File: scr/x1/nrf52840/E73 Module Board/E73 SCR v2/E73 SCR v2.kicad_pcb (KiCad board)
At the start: 4 copper layers, 50 x 35 mm, 36 parts, among them J1 SWD, J2 USB_B_Micro, J3 XC1, J4 XC2, J5 XC3, J6 BAT, Q1 AO3401, SW1 SW_BAT, U1 E73-2G4M08S1C-52840, U2 MCP73831-2-OT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

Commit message: Auto stash before merge of "footprint_update" and "origin/footprint_update"
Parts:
- RST1: footprint Switches:Tac_SPST_RightAngle_SideActuated_THT -> Switches:Tac_SMD_6.4mm_Side_SPST_NO
- moved RST1 22.5 mm to (71.2, 122.5)
- moved R6 4.37 mm to (112.0, 103.5), turned to 180 degrees
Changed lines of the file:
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@@
     (add_net "Net-(D1-Pad3)")
     (add_net "Net-(D2-Pad1)")
+    (add_net "Net-(D3-Pad1)")
     (add_net "Net-(D4-Pad1)")
+    (add_net "Net-(J1-Pad6)")
+    (add_net "Net-(J1-Pad7)")
+    (add_net "Net-(J1-Pad8)")
+    (add_net "Net-(J2-Pad4)")
     (add_net "Net-(J2-Pad6)")
     (add_net "Net-(R7-Pad2)")
@@
     (add_net P1.02)
     (add_net P1.09)
+    (add_net P1_11)
     (add_net RESET)
     (add_net SPKR)
@@
     (uvia_drill 0.1)
     (add_net VBUS)
+  )
+  (module Switches:Tac_SMD_6.4mm_Side_SPST_NO (layer F.Cu)
+    (at 71.25 122.5)
+    (descr "side smd tac switch")
+    (tags "switch tac rightangle side smd")
+    (attr smd)
+    (fp_text reference RST1 (at 0 0) (layer F.Fab)
+      (effects (font (size 1 1) (thickness 0.15)))
+    )
+    (fp_text value SW_SPST (at 0 -2.7) (layer F.Fab)
+      (effects (font (size 1 1) (thickness 0.15)))
+    )
+    (fp_line (start -1.3 2.5) (end 1.3 2.5) (layer Eco1.User) (width 0.15))
+    (fp_line (start 1.3 2.75) (end 1.3 1.75) (layer Eco1.User) (width 0.15))
+    (fp_line (start -1.3 2.75) (end 1.3 2.75) (layer Eco1.User) (width 0.15))
+    (fp_line (start -1.3 1.75) (end -1.3 2.75) (layer Eco1.User) (width 0.15))
+    (fp_line (start -3.4 1.75) (end -3.4 -1.7) (layer F.SilkS) (width 0.15))
+    (fp_line (start 3.4 1.75) (end -3.4 1.75) (layer F.SilkS) (width 0.15))
+    (fp_line (start 3.4 -1.75) (end 3.4 1.75) (layer F.SilkS) (width 0.15))
+    (fp_line (start -3.4 -1.75) (end 3.4 -1.75) (layer F.SilkS) (width 0.15))
+    (pad 1 smd rect (at 2.8 -0.85) (size 1.2 1) (layers F.Cu F.Paste F.Mask)
+      (net 1 GND))
+    (pad 2 smd rect (at 2.8 0.85) (size 1.2 1) (layers F.Cu F.Paste F.Mask)
+      (net 10 RESET))
+    (pad 2 smd rect (at -2.8 0.85) (size 1.2 1) (layers F.Cu F.Paste F.Mask)
+      (net 10 RESET))
+    (pad 1 smd rect (at -2.8 -0.75) (size 1.2 1) (layers F.Cu F.Paste F.Mask)
+      (net 1 GND))
+    (pad "" np_thru_hole circle (at 0 1.375) (size 0.75 0.75) (drill 0.75) (layers *.Cu *.Mask))
+    (pad "" np_thru_hole circle (at 0 -1.375) (size 0.75 0.75) (drill 0.75) (layers *.Cu *.Mask))
   )
   (module BVH_Components_Misc:SMD_Speaker (layer F.Cu)
@@
       (net 1 GND))
   )
-  (module Switches:Tac_SPST_RightAngle_SideActuated_THT (layer F.Cu)
-    (at 93.75 121.5)
-    (fp_text reference RST1 (at 0 2.9) (layer F.SilkS)
-      (effects (font (size 1 1) (thickness 0.15)))
-    )
-    (fp_text value SW_SPST (at -0.1 -0.2) (layer F.Fab)
-      (effects (font (size 1 1) (thickness 0.15)))
-    )
-    (fp_line (start -1.75 6.25) (end -1.75 2) (layer F.CrtYd) (width 0.15))
-    (fp_line (start 1.75 6.25) (end 1.75 2) (layer F.CrtYd) (width 0.15))
-    (fp_text user "Button Front" (at 0.05 5.65) (layer Dwgs.User)
-      (effects (font (size 1 1) (thickness 0.15)))
-    )
-    (fp_line (start -1.75 6.25) (end 1.75 6.25) (layer F.CrtYd) (width 0.15))
-    (fp_line (start -5 2) (end -5 -3.45) (layer F.CrtYd) (width 0.15))
-    (fp_line (start 5 2) (end -5 2) (layer F.CrtYd) (width 0.15))
-    (fp_line (start 4.95 -3.5) (end 4.95 2) (layer F.CrtYd) (width 0.15))
-    (fp_line (start -5 -3.5) (end 4.95 -3.5) (layer F.CrtYd) (width 0.15))
-    (pad "" thru_hole oval (at 3.5 -1.25) (size 2 2.5) (drill 1.3) (layers *.Cu *.Mask))
-    (pad 2 thru_hole oval (at 2.25 1.25) (size 1.5 1.5) (drill 1) (layers *.Cu *.Mask)
-      (net 10 RESET))
-    (pad "" thru_hole oval (at -3.5 -1.25) (size 2 2.5) (drill 1.3) (layers *.Cu *.Mask))
-    (pad 1 thru_hole oval (at -2.25 1.24) (size 1.5 1.5) (drill 1) (layers *.Cu *.Mask)
-      (net 1 GND))
-  )
   (module Resistors_SMD:R_0805_HandSoldering (layer F.Cu)
     (at 116.25 113.75 180)
@@
   )
   (module Resistors_SMD:R_0805_HandSoldering (layer F.Cu)
-    (at 116.1 102)
+    (at 112 103.5 180)
     (descr "Resistor SMD 0805, hand soldering")
     (tags "resistor 0805")
@@
     (fp_line (start 2.35 0.9) (end 2.35 -0.9) (layer F.CrtYd) (width 0.05))
     (fp_line (start 2.35 0.9) (end -2.35 0.9) (layer F.CrtYd) (width 0.05))
-    (pad 1 smd rect (at -1.35 0) (size 1.5 1.3) (layers F.Cu F.Paste F.Mask)
+    (pad 1 smd rect (at -1.35 0 180) (size 1.5 1.3) (layers F.Cu F.Paste F.Mask)
       (net 13 BATSENSE))
-    (pad 2 smd rect (at 1.35 0) (size 1.5 1.3) (layers F.Cu F.Paste F.Mask)
+    (pad 2 smd rect (at 1.35 0 180) (size 1.5 1.3) (layers F.Cu F.Paste F.Mask)
       (net 1 GND))
     (model ${KISYS3DMOD}/Resistors_SMD.3dshapes/R_0805.wrl

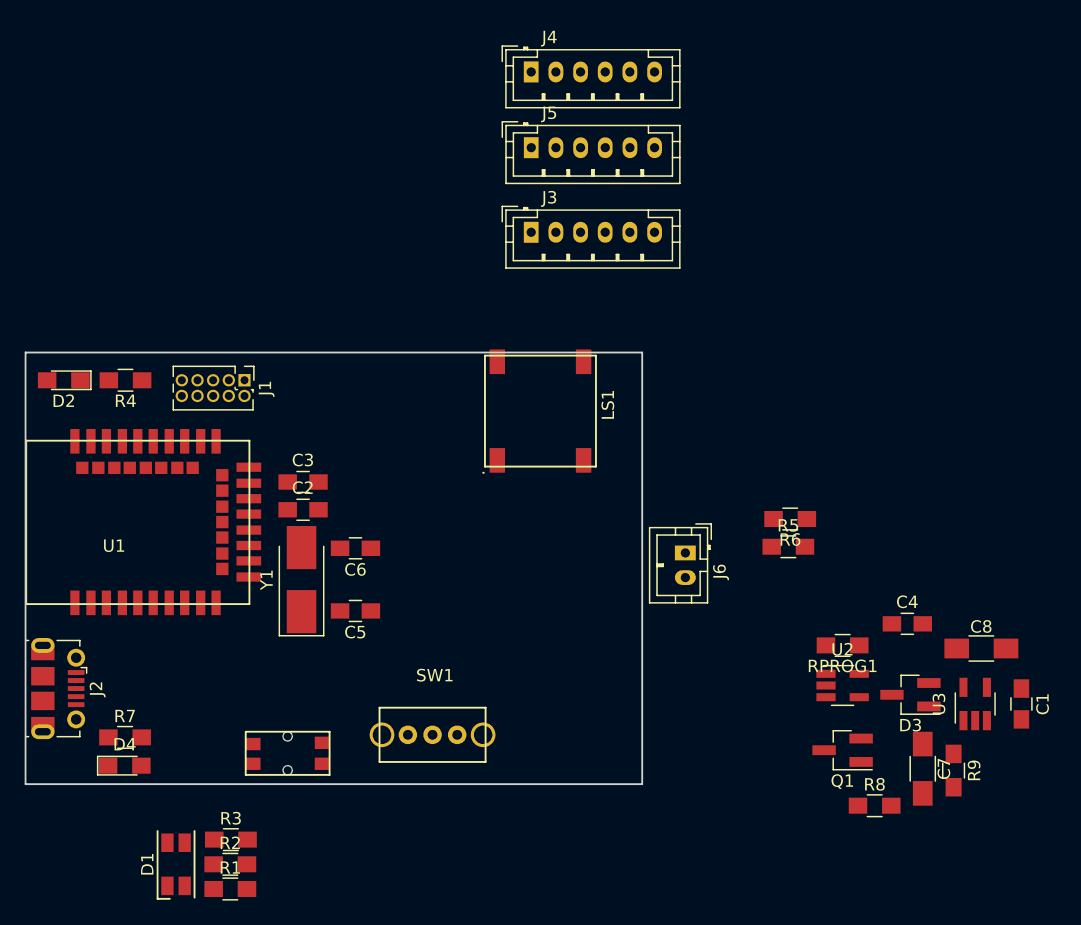
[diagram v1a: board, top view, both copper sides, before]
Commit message: Layout WIP - Floor planning and copper pours
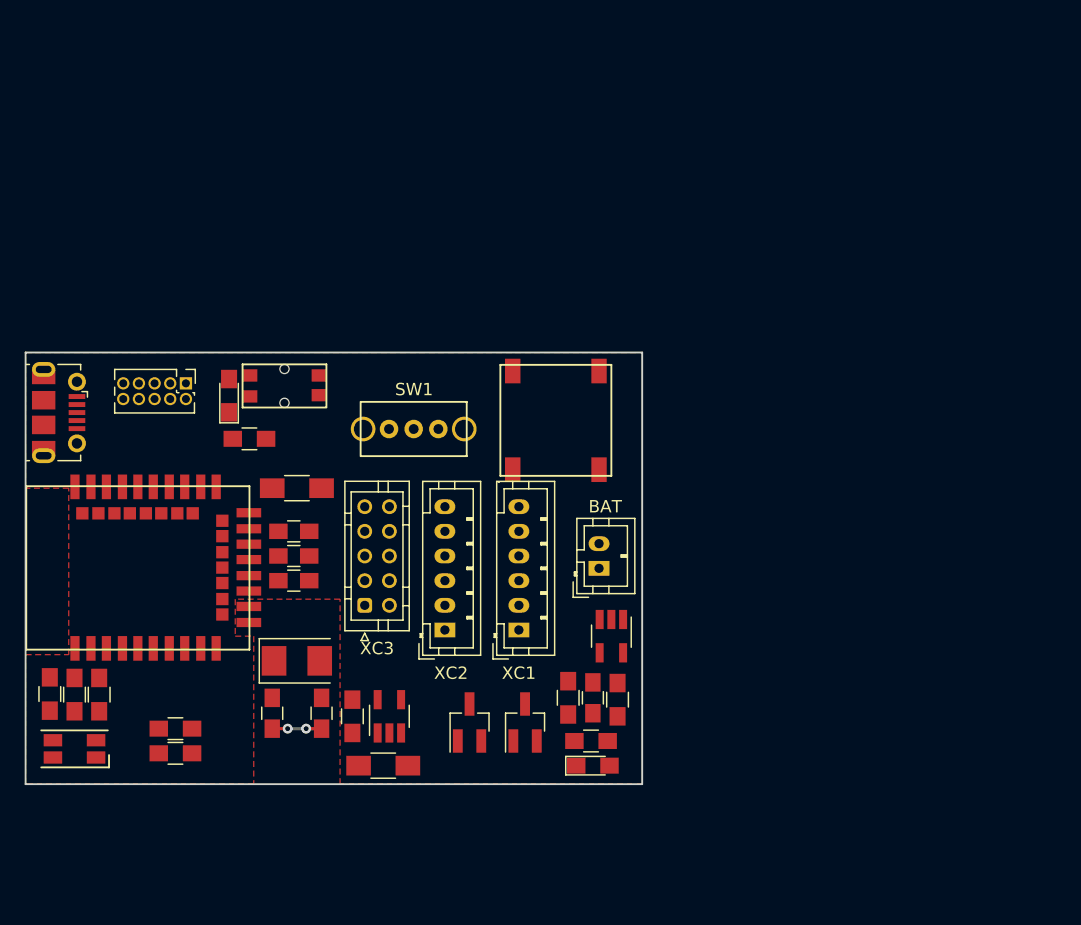
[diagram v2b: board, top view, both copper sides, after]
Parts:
- U1: footprint BVH_nrf52_Modules:E73(2G4M08S1C)-HandSoldered -> BVH_NRF52_Modules:E73(2G4M08S1C)-HandSoldered
- XC3: renamed from J5; footprint Connectors_JST:JST_PH_B6B-PH-K_06x2.00mm_Straight -> Connector_JST:JST_PHD_B10B-PHDSS_2x05_P2.00mm_Vertical
- Y1: footprint Crystals:Crystal_SMD_5032-2pin_5.0x3.2mm_HandSoldering -> Crystal:Crystal_SMD_5032-2Pin_5.0x3.2mm
- moved C1 59.8 mm to (71.8, 108.5), turned to 0 degrees
- moved C8 57.0 mm to (72.0, 101.0)
- moved R6 52.7 mm to (62.1, 120.5)
- moved R5 52.4 mm to (62.1, 122.5)
- moved R9 48.9 mm to (76.5, 119.5), turned to 90 degrees
- moved U3 47.5 mm to (79.5, 119.5)
- moved XC2 45.8 mm to (84.0, 112.5), turned to 90 degrees
- moved C7 43.8 mm to (79.0, 123.5), turned to 0 degrees
- moved XC3 39.5 mm to (77.5, 110.5), turned to 90 degrees
- moved D4 38.0 mm to (96.0, 123.5)
- moved R7 37.8 mm to (95.8, 121.5)
- moved D3 35.8 mm to (86.0, 120.0), turned to 90 degrees
- moved XC1 32.3 mm to (90.0, 112.5), turned to 90 degrees
- moved RST1 29.8 mm to (71.0, 92.7), turned to 180 degrees
- moved R8 26.3 mm to (94.0, 118.0), turned to 270 degrees
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- renumbered J6 to BAT, J3 to XC1, J4 to XC2
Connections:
- U1 pad 1: (no net) -> LED_B
- U1 pad 10: LED_R -> (no net)
- U1 pad 12: (no net) -> P0.26
- U1 pad 14: (no net) -> P0.06
- U1 pad 2: (no net) -> LED_G
- U1 pad 3: (no net) -> LED_R
- U1 pad 32: (no net) -> P0.20
- U1 pad 33: (no net) -> P0.13
- U1 pad 8: LED_B -> (no net)
- U1 pad 9: LED_G -> (no net)
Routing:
- net GND: track 0.00 -> 5.50 mm, vias 0 -> 2
- net D+: track 0.00 -> 0.61 mm
- added copper zone on In2.Cu, net +3V3
- added copper zone on F.Cu, net GND
- added copper zone on In1.Cu, net GND

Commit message: Routing and layout almost complete
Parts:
- removed BAT: BAT, Connectors_JST:JST_PH_B2B-PH-K_02x2.00mm_Straight
- added G***: LOGO, BVH_Logos:SkyIron_logo_Back, F.Cu at (63.0, 111.0)
- added J6: BAT, Connectors_JST:JST_PH_B2B-PH-K_02x2.00mm_Straight, F.Cu at (96.5, 107.5)
- added REF**: MountingHole_2.2mm_M2, Mounting_Holes:MountingHole_2.2mm_M2, F.Cu at (61.0, 120.5)
- Y1: footprint Crystal:Crystal_SMD_5032-2Pin_5.0x3.2mm -> Crystals:Crystal_SMD_5032-2pin_5.0x3.2mm_HandSoldering
- moved R5 26.3 mm to (88.4, 122.8), turned to 180 degrees
- moved R6 21.6 mm to (83.6, 122.8)
- moved R7 4.39 mm to (98.5, 118.0), turned to 90 degrees
- moved R8 3.40 mm to (92.0, 120.8)
- moved C4 3.26 mm to (94.2, 120.8)
- moved RPROG1 3.21 mm to (95.2, 116.5), turned to 180 degrees
- moved D4 2.76 mm to (96.2, 120.8), turned to 90 degrees
- moved Q1 2.70 mm to (89.0, 117.8)
- moved D3 2.46 mm to (85.0, 117.8)
- moved C7 1.23 mm to (77.8, 123.2)
- moved U3 1.12 mm to (80.5, 119.0)
- moved C1 0.71 mm to (72.2, 109.0)
- moved C3 0.71 mm to (72.2, 104.0)
- moved J2 0.63 mm to (51.8, 95.5)
- moved C2 0.50 mm to (72.2, 106.5)
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- renumbered XC1 to J3, XC2 to J4, XC3 to J5
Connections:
- J3 pad 5: P0.08 -> P1.02
- J3 pad 6: P1.09 -> P0.13
- J4 pad 3: P.04_A2 -> P0.17
- J4 pad 4: P0.12 -> P0.20
- J4 pad 5: P0.07 -> P0.22
- J4 pad 6: P0.15 -> P1.00
- J5 pad 10: P0.13 -> P0.15
- J5 pad 3: P0.22 -> P0.26
- J5 pad 4: P1.00 -> P0.06
- J5 pad 5: P1.02 -> P0.08
- J5 pad 6: P0.24 -> P1.09
- J5 pad 7: P0.26 -> P.04_A2
- J5 pad 8: P0.06 -> P0.12
- J5 pad 9: P0.20 -> P0.07
- U1 pad 30: SPKR -> P0.17
- U1 pad 35: P0.24 -> SPKR
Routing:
- net VBUS: track 0.00 -> 101.3 mm, vias 0 -> 3
- net P0.28_A4: track 0.00 -> 45.4 mm, vias 0 -> 1
- net SPKR: track 0.00 -> 41.5 mm, vias 0 -> 2
- net P1.02: track 0.00 -> 37.1 mm, vias 0 -> 1
- net P0.13: track 0.00 -> 33.9 mm, vias 0 -> 1
- net BATSENSE: track 0.00 -> 33.2 mm, vias 0 -> 2
- net +BATT: track 0.00 -> 30.1 mm, vias 0 -> 2
- net P0.22: track 0.00 -> 29.9 mm, vias 0 -> 1
- net P1.00: track 0.00 -> 29.6 mm, vias 0 -> 1
- net P0.20: track 0.00 -> 29.1 mm, vias 0 -> 1
- net P0.05_A3: track 0.00 -> 28.6 mm, vias 0 -> 1
- net P0.17: track 0.00 -> 28.3 mm, vias 0 -> 1
- net Net-(SW1-Pad2): track 0.00 -> 25.4 mm
- net RESET: track 0.00 -> 25.1 mm
- net Net-(R9-Pad2): track 0.00 -> 24.9 mm
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- added copper zone on B.Cu, net GND
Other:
- outline, holes or cut-outs redrawn
- net class VBUS: clearance 0.25 -> 0.3; via_dia 0.8 -> 1
- board text added: "BVH - AB4EN nRF52840 Breakout v2 2020-06"

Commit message: v2 fully routed and ready for submission
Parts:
- C8: footprint Capacitors_SMD:C_1206_HandSoldering -> Capacitors_SMD:C_0805_HandSoldering
- moved C8 16.5 mm to (79.8, 115.5)
- moved C1 3.70 mm to (72.2, 105.3)
- moved C2 0.70 mm to (72.2, 107.2)
- moved C3 0.55 mm to (72.2, 103.5)
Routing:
- net GND: track 12.3 -> 16.3 mm, vias 96 -> 101
- net LED_1: track 14.7 -> 18.5 mm
- net Net-(R9-Pad2): track 24.9 -> 26.7 mm
- net XL1: track 7.02 -> 8.06 mm
- net P0.28_A4: track 45.4 -> 44.5 mm
- net D+: track 10.9 -> 11.6 mm
- net XL2: track 10.6 -> 11.4 mm
- net +3V3: track 20.0 -> 19.6 mm, vias 5 -> 6
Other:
- net class USB added: clearance 0.1524, trace_width 0.2286, via_dia 0.8, via_drill 0.4
- rule trace_min: 0.2 -> 0.127
